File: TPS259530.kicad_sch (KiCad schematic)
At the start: 19 parts, among them Q4 2N7002, U4 TPS259530DSGR

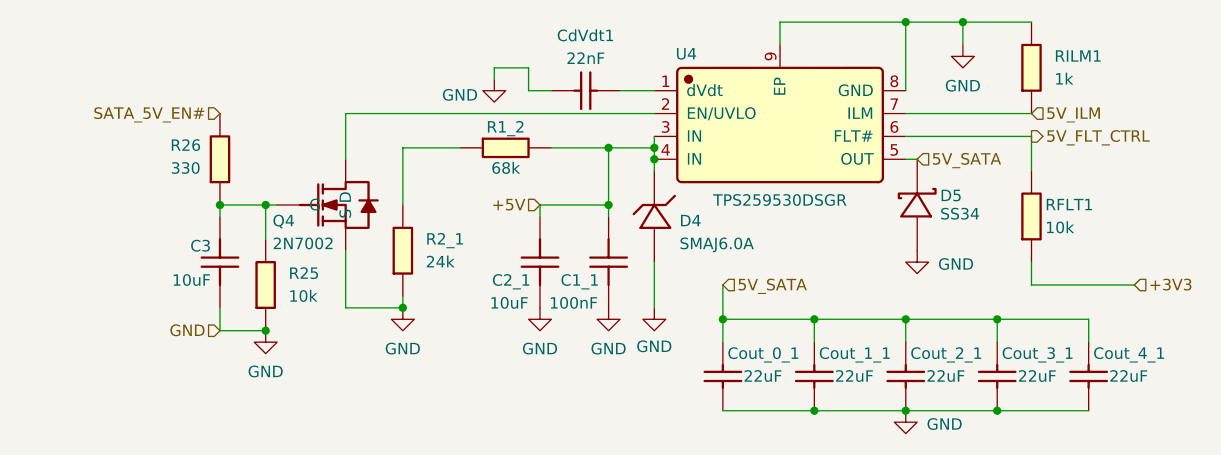
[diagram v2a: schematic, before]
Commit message: Basic Function Review/Documentation for LT6911C Subsystem
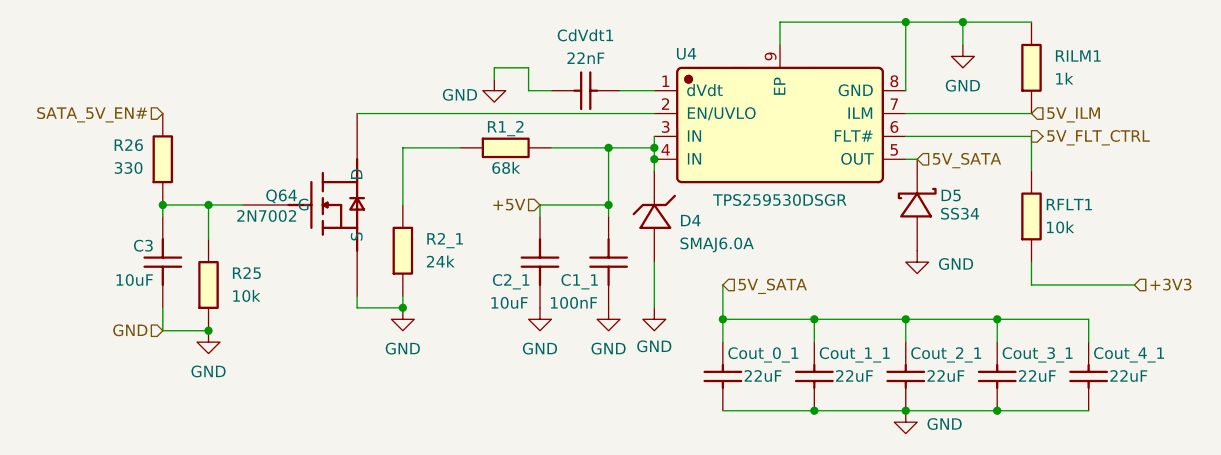
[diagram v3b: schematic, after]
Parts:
- removed Q4: 2N7002, Package_TO_SOT_SMD:SOT-23-3, symbol JLCImport:2N7002
- added Q64: 2N7002, JLCImport:2N7002_C916396, symbol JLCImport:2N7002_C916396
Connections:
- net GND: now also Q64.2 (S)
- net at C3.2, R25.2, R26.1: now also Q64.1 (G)
- net at U4.2 (EN/UVLO): now also Q64.3 (D)
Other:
- moved on the sheet: C3, R25, R26
